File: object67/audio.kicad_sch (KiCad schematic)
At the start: 56 parts, among them IC1 AK4493SEQ, IC2 TAA5242IRGER, IC3 LMK1C1104PWR, U1 RCJ-2223, Y3 ASDLJ-E-49.152MHZ-L-R-T, Y4 ASDLJ-E-45.1584MHz-L-R-T

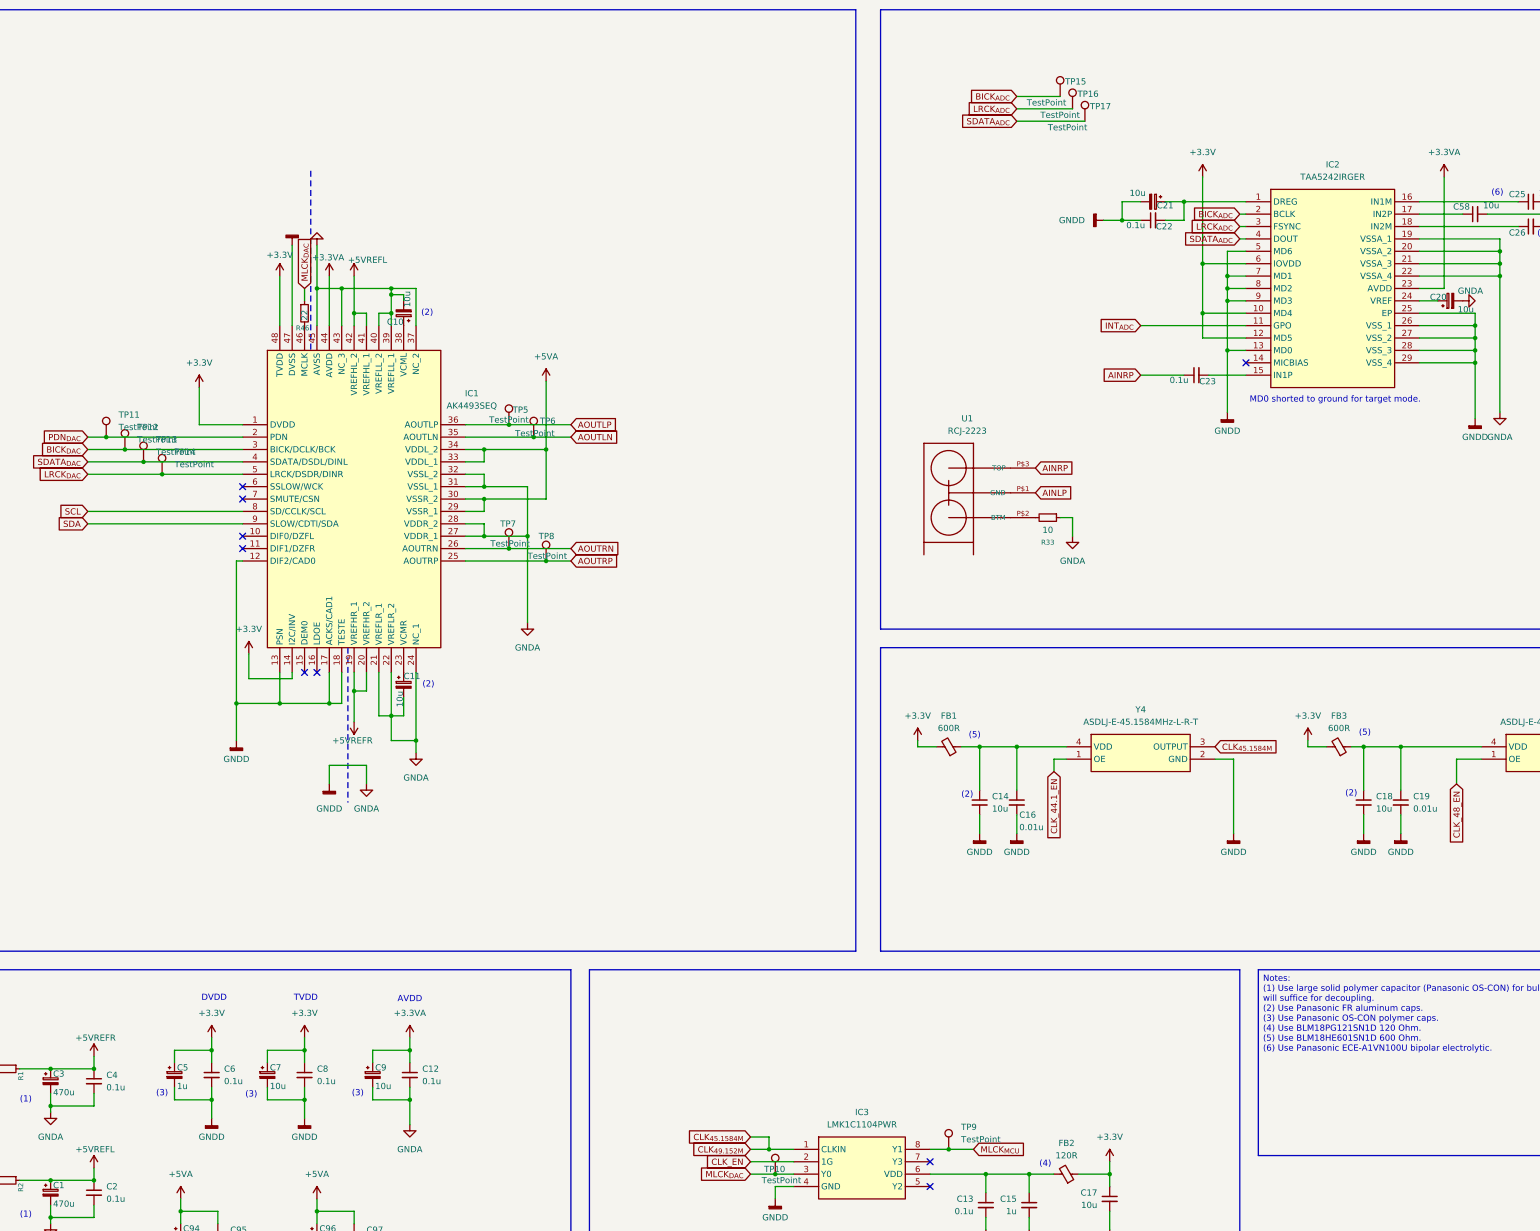
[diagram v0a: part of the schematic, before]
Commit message: Finished layout for ADC DAC, starting filter
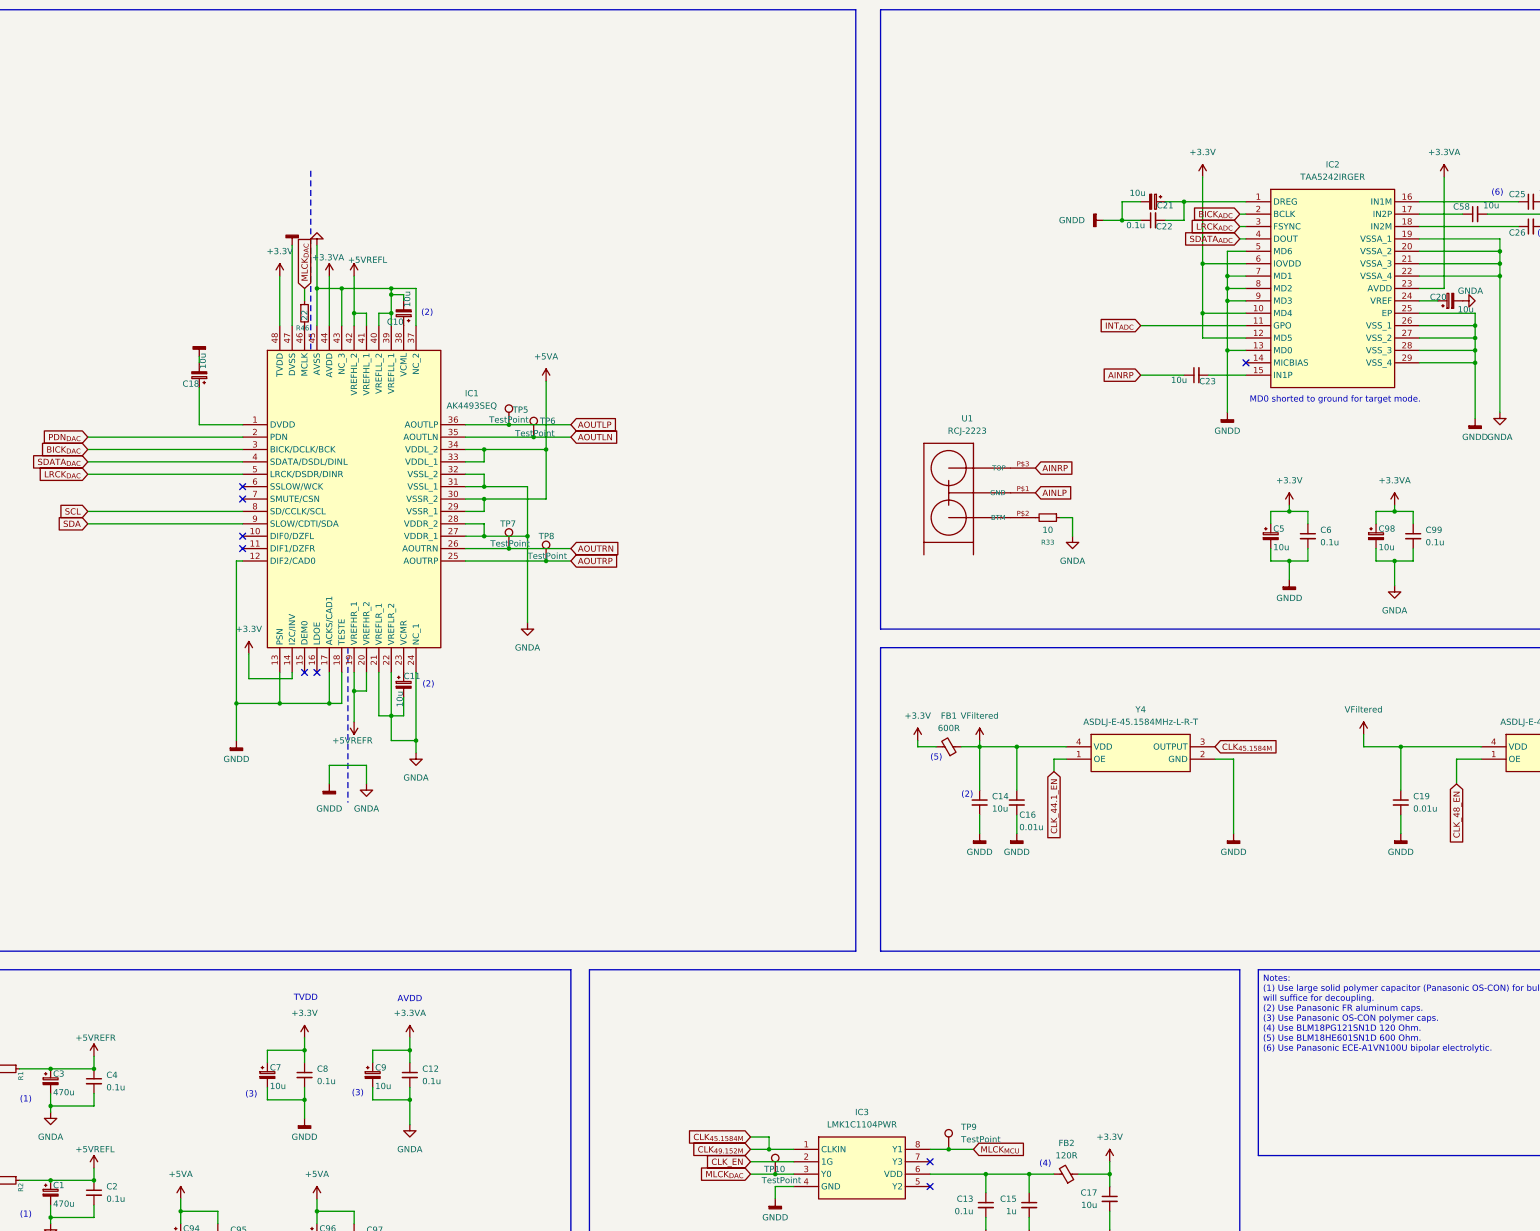
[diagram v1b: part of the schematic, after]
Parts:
- removed C18: 10u, Capacitor_SMD:CP_Elec_4x5.3, symbol Device:C_Small
- removed FB3: 600R, Inductor_SMD:L_0603_1608Metric, symbol Device:FerriteBead_Small
- removed TP11, TP12, TP13, TP14, TP15, TP16, TP17: TestPoint, TestPoint:TestPoint_Pad_D2.0mm, symbol Connector:TestPoint
- added C18, C98: 10u, Capacitor_SMD:CP_Elec_4x5.3, symbol Device:C_Polarized_Small
- added C99: 0.1u, Capacitor_SMD:C_0603_1608Metric, symbol Device:C_Small
- C23: value 0.1u -> 10u
- C5: value 1u -> 10u; footprint Capacitor_SMD:C_1206_3216Metric -> Capacitor_SMD:CP_Elec_4x5.3
- C6: footprint Capacitor_SMD:C_0402_1005Metric -> Capacitor_SMD:C_0603_1608Metric
- TP10, TP5, TP6, TP7, TP8, TP9: footprint TestPoint:TestPoint_Pad_D2.0mm -> TestPoint:TestPoint_Pad_D1.0mm
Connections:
- net +3.3V: no longer IC1.1 (DVDD)
- net +3.3VA: now also C98.1, C99.1
- net GNDA: now also C18.2, C98.2, C99.2
- net VFiltered: now reaches C14.1, C16.1, FB1.1, Y4.4 (VDD)
- net VFiltered: now also C19.1, Y3.4 (VDD)
- new net: C18.1, IC1.1 (DVDD)
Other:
- note removed: "DVDD"

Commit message: Finished layout, start MCU
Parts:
- removed TP9: TestPoint, TestPoint:TestPoint_Pad_D1.0mm, symbol Connector:TestPoint
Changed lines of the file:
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@@
 	)
 	(junction
-		(at 236.22 247.65)
-		(diameter 0)
-		(color 0 0 0 0)
-	)
-	(junction
 		(at 121.92 71.12)
 		(diameter 0)
@@
 	(wire
 		(pts
-			(xy 236.22 247.65) (xy 232.41 247.65)
+			(xy 232.41 247.65) (xy 241.3 247.65)
 		)
 		(stroke
@@
 	(wire
 		(pts
-			(xy 241.3 247.65) (xy 236.22 247.65)
-		)
-		(stroke
-			(width 0)
-			(type default)
-		)
-	)
-	(wire
-		(pts
 			(xy 252.73 252.73) (xy 243.84 252.73)
 		)
@@
 					(unit 1)
 				)
-			)
-		)
-	)
-	(symbol
-		(lib_id "Connector:TestPoint")
-		(at 236.22 247.65 0)
-		(unit 1)
-		(exclude_from_sim no)
-		(in_bom yes)
-		(on_board yes)
-		(dnp no)
-		(fields_autoplaced yes)
-		(property "Reference" "TP9"
-			(at 238.76 243.0779 0)
-			(effects
-				(font
-					(size 1.27 1.27)
-				)
-				(justify left)
-			)
-		)
-		(property "Value" "TestPoint"
-			(at 238.76 245.6179 0)
-			(effects
-				(font
-					(size 1.27 1.27)
-				)
-				(justify left)
-			)
-		)
-		(property "Footprint" "TestPoint:TestPoint_Pad_D1.0mm"
-			(at 241.3 247.65 0)
-			(effects
-				(font
-					(size 1.27 1.27)
-				)
-				(hide yes)
-			)
-		)
-		(property "Datasheet" "~"
-			(at 241.3 247.65 0)
-			(effects
-				(font
-					(size 1.27 1.27)
-				)
-				(hide yes)
-			)
-		)
-		(property "Description" "test point"
-			(at 236.22 247.65 0)
-			(effects
-				(font
-					(size 1.27 1.27)
-				)
-				(hide yes)
-			)
-		)
-		(pin "1"
-		)
-		(instances
-			(project "object67"
-				(path "/a52a93a9-ab60-414c-847b-3047ce4056cf/2d7be8e2-05a1-49f5-8994-604be09973f2/f43f4198-176f-4b92-97fe-5a3f8cda9d3b"
-					(reference "TP9")
-					(unit 1)
-				)

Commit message: LAyout
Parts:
- added R48, R52, R53, R54: 22, Resistor_SMD:R_0402_1005Metric, symbol Device:R_Small
- C3: footprint Capacitor_THT:CP_Radial_D8.0mm_P3.50mm -> Capacitor_THT:CP_Radial_D8.0mm_P5.00mm
- R46: footprint Capacitor_SMD:C_0201_0603Metric -> Resistor_SMD:R_0402_1005Metric
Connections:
- net BICK_{ADC}: now also R52.2; no longer IC2.2 (BCLK)
- net CLK_{45.1584M}: now also R46.1, R48.1; no longer Y3.3 (OUTPUT), Y4.3 (OUTPUT)
- net LRCK_{ADC}: now also R53.2; no longer IC2.3 (FSYNC)
- net MLCK_{DAC}: now also IC1.46 (MCLK); no longer R46.1
- net SDATA_{ADC}: now also R54.2; no longer IC2.4 (DOUT)
- net at R46.2: now also Y4.3 (OUTPUT); no longer IC1.46 (MCLK)
- new net: R48.2, Y3.3 (OUTPUT)
- new net: IC2.2 (BCLK), R52.1
- new net: IC2.3 (FSYNC), R53.1
- new net: IC2.4 (DOUT), R54.1
